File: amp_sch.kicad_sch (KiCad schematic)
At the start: 10 parts, among them IC1 AD7730, U1 74LVC125APW,118

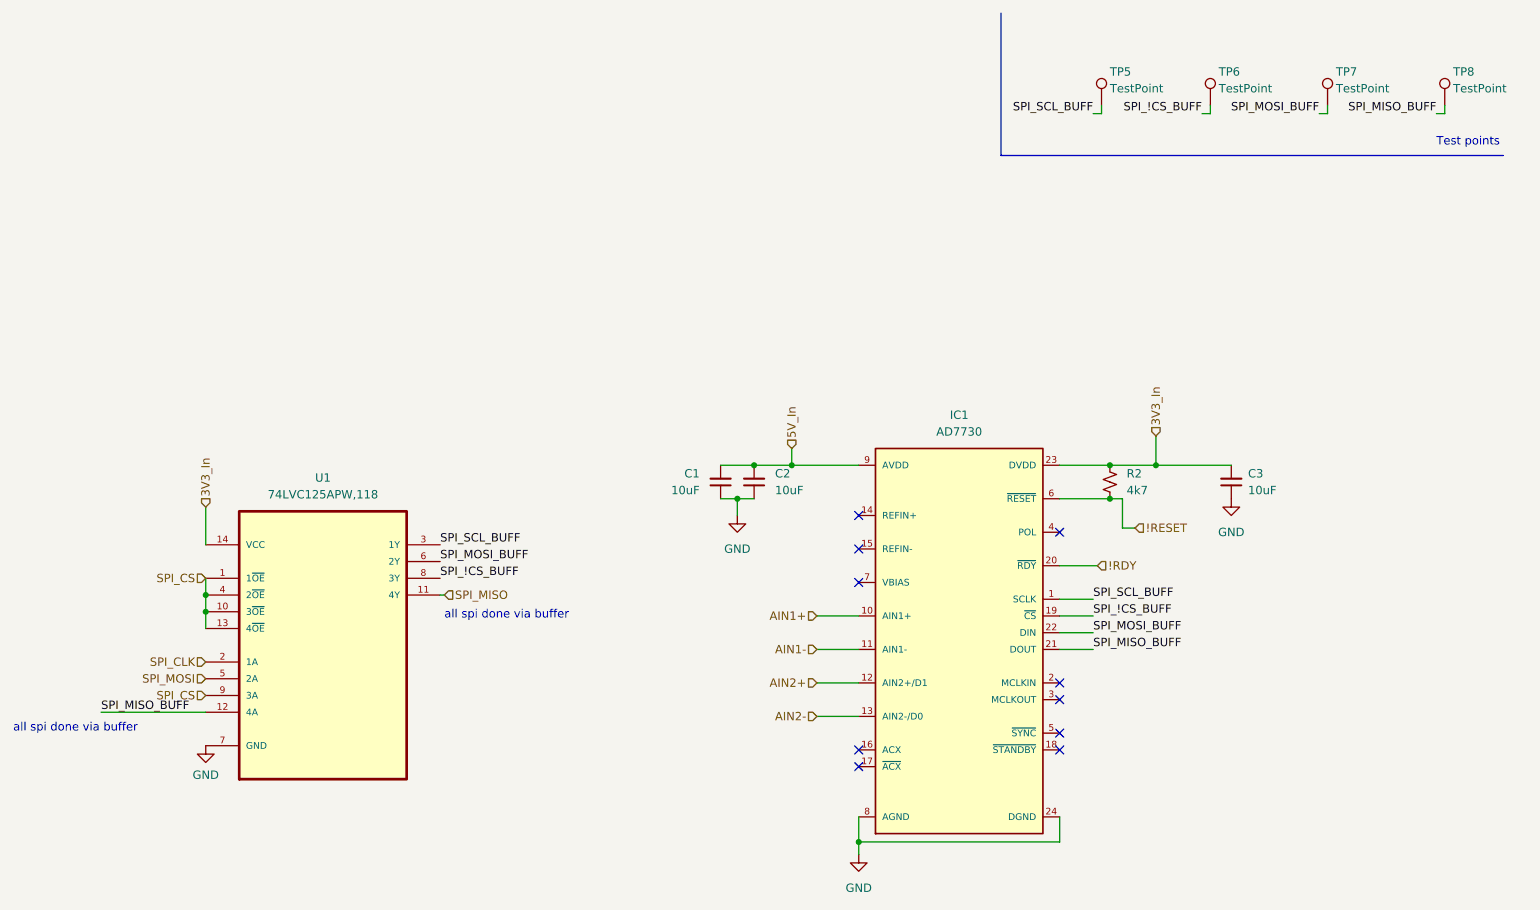
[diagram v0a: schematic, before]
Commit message: Changes to the AD7730 based on Montso's working Arduino system
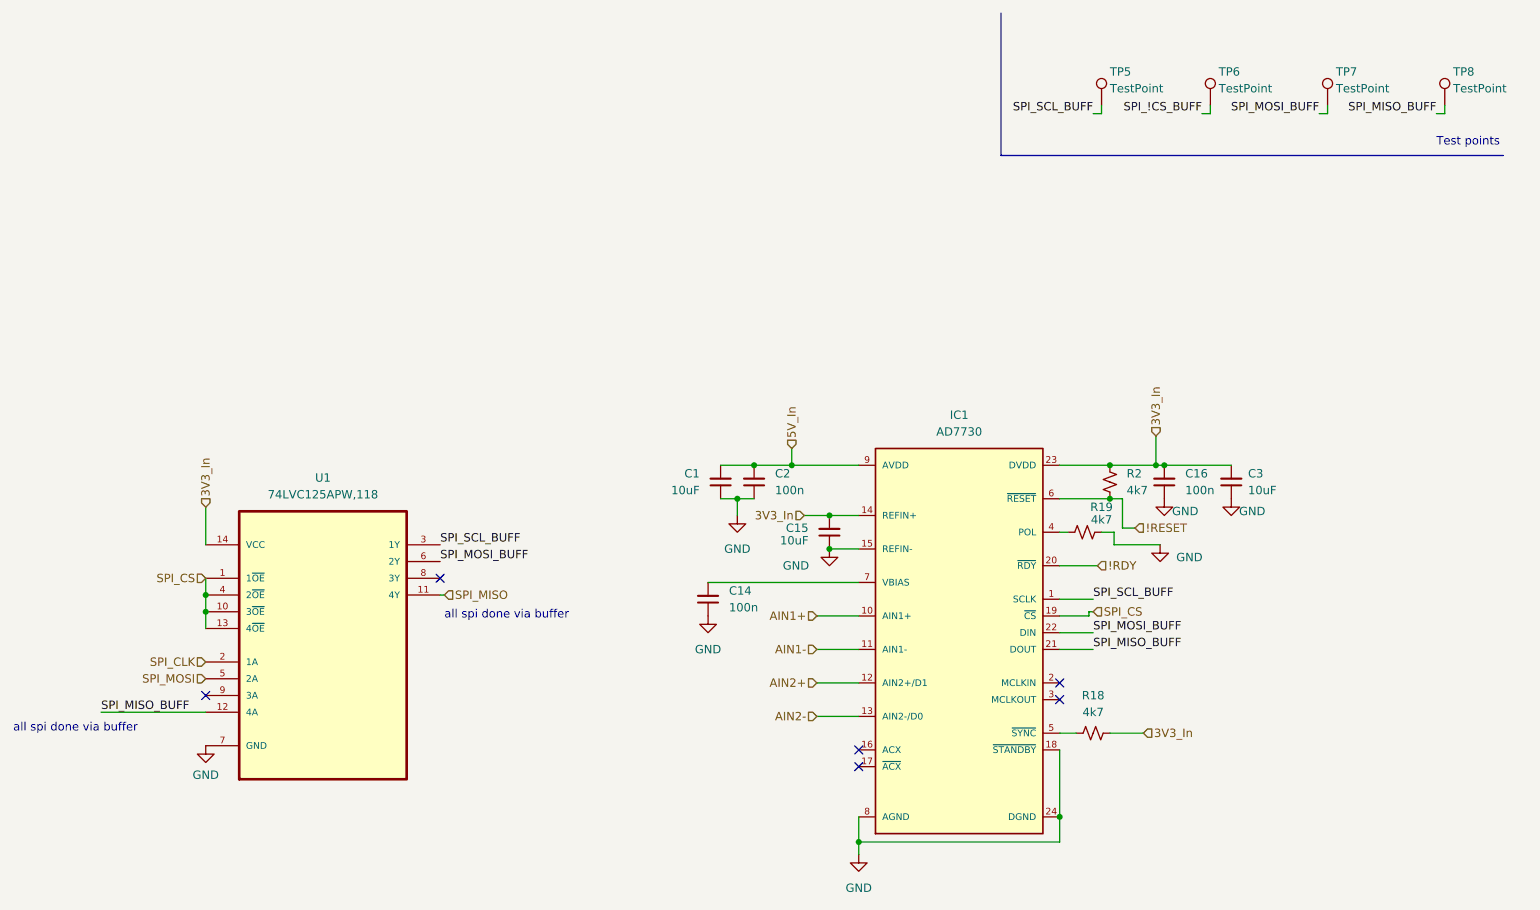
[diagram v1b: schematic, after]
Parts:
- added C14, C16: 100n, Capacitor_SMD:C_0603_1608Metric, symbol Device:C_Small
- added C15: 10uF, Capacitor_SMD:C_0603_1608Metric, symbol Device:C_Small
- added R18, R19: 4k7, Resistor_SMD:R_0402_1005Metric, symbol Device:R_Small_US
- C2: value 10uF -> 100n; LCSC C96446 -> (none); Price 0.024 -> (none)
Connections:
- net 3V3_In: now also IC1.14 (REFIN+), C15.2, C16.2, R18.1
- net GND: now also IC1.15 (REFIN-), IC1.18 (~{STANDBY}), C14.1, C15.1, C16.1, R19.1
- net SPI_!CS_BUFF: no longer IC1.19 (~{CS}), U1.8 (3Y)
- net SPI_CS: now also IC1.19 (~{CS}); no longer U1.9 (3A)
- net at IC1.4 (POL): now also R19.2
- net at IC1.5 (~{SYNC}): now also R18.2
- net at IC1.7 (VBIAS): now also C14.2
- no-connect marks 10 -> 6

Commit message: Changes made to the AD7730 circuit. HX711 circuit added and AD7730 sidestepped.
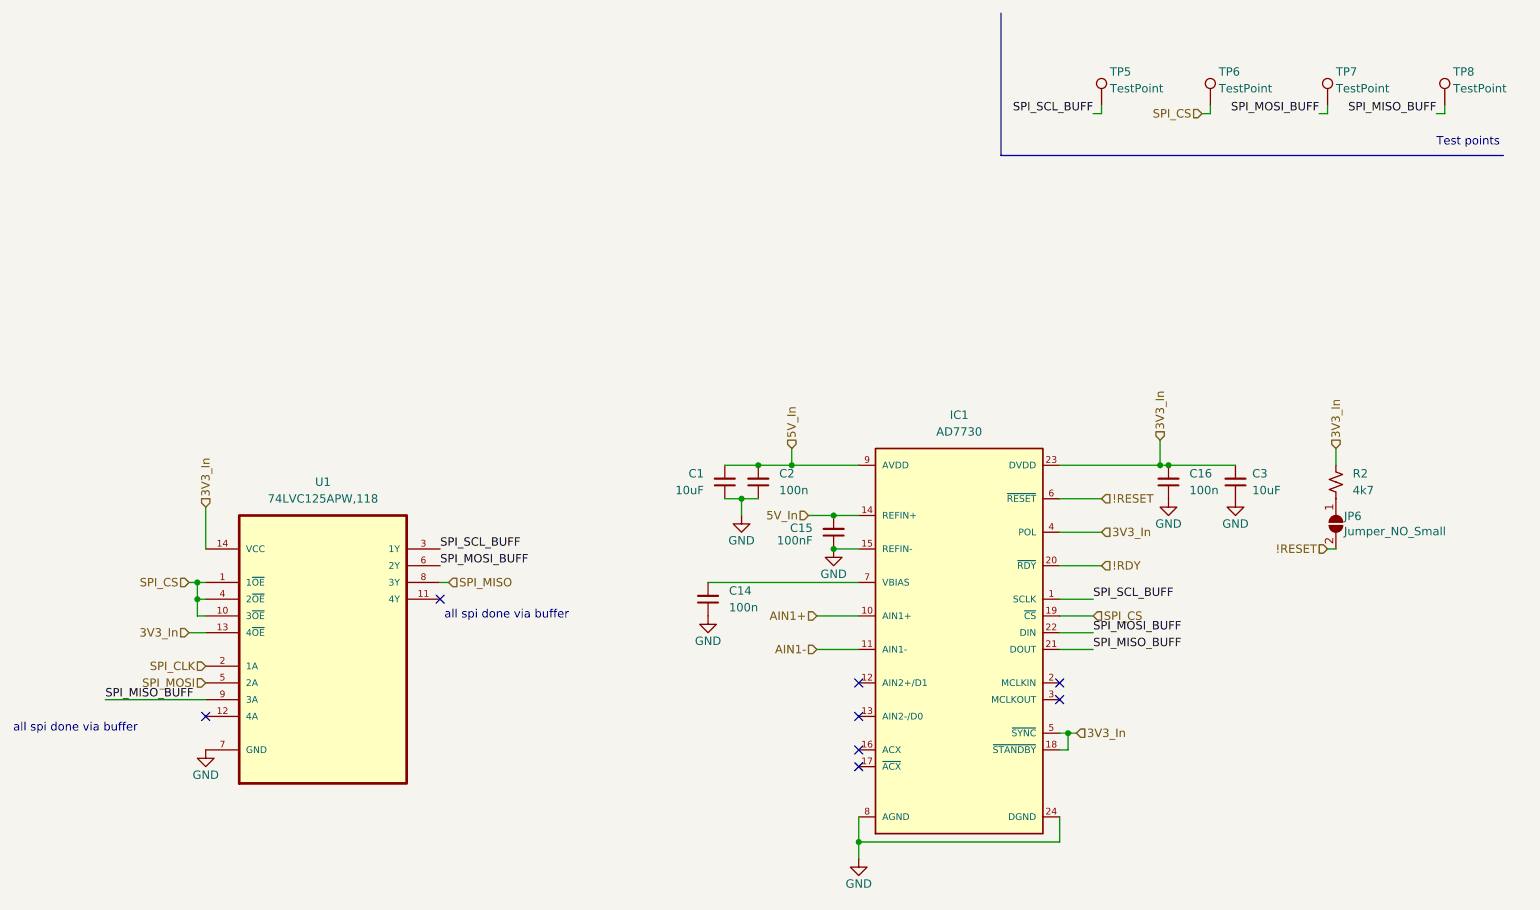
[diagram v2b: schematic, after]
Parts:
- removed R18, R19: 4k7, Resistor_SMD:R_0402_1005Metric, symbol Device:R_Small_US
- added JP6: Jumper_NO_Small, Jumper:SolderJumper-2_P1.3mm_Open_RoundedPad1.0x1.5mm, symbol Jumper:SolderJumper_2_Open
- C15: value 10uF -> 100nF
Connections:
- net SPI_!CS_BUFF is gone; now on net SPI_CS: TP6.1
- net !RESET: now also JP6.2 (B); no longer R2.1
- net 3V3_In: now also IC1.18 (~{STANDBY}), IC1.4 (POL), IC1.5 (~{SYNC}), U1.13 (4~{OE}); no longer C15.2, IC1.14 (REFIN+)
- net 5V_In: now also C15.2, IC1.14 (REFIN+)
- net GND: no longer IC1.18 (~{STANDBY})
- net SPI_CS: no longer U1.13 (4~{OE})
- net SPI_MISO: now also U1.8 (3Y); no longer U1.11 (4Y)
- net SPI_MISO_BUFF: now also U1.9 (3A); no longer U1.12 (4A)
- net AIN2+: no longer names the net of IC1.12 (AIN2+/D1)
- net AIN2-: no longer names the net of IC1.13 (AIN2-/D0)
- new net: JP6.1 (A), R2.1
- no-connect marks 6 -> 8
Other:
- moved on the sheet: C1, C15, C16, C2, C3, R2, U1

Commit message: Added footprints for HX711 circuit on PCB and modified pin assignment
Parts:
- U1: symbol 74LVC125A:74LVC125APW,118 -> 74LVC125APW_118:74LVC125APW,118
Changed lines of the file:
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@@
     )
   )
-  (symbol (lib_id "74LVC125A:74LVC125APW,118") (at 102.87 107.95 0) (unit 1)
+  (symbol (lib_id "74LVC125APW_118:74LVC125APW,118") (at 102.87 107.95 0) (unit 1)
     (in_bom yes) (on_board yes) (dnp no) (fields_autoplaced)
     (property "Reference" "U1" (at 102.87 85.09 0)

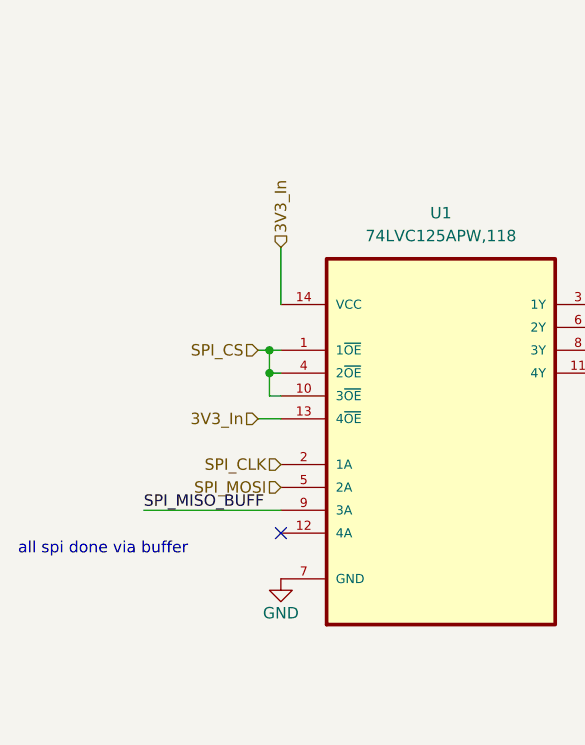
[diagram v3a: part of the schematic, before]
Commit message: Updated +3V3 tracks on pcb and buffer schematic
-Added decoupling cap for buffer
-Tied unused buffer input 4 to gnd
-Did all +3V3 connections
-Fixed +5V tracks
-gnd stitching
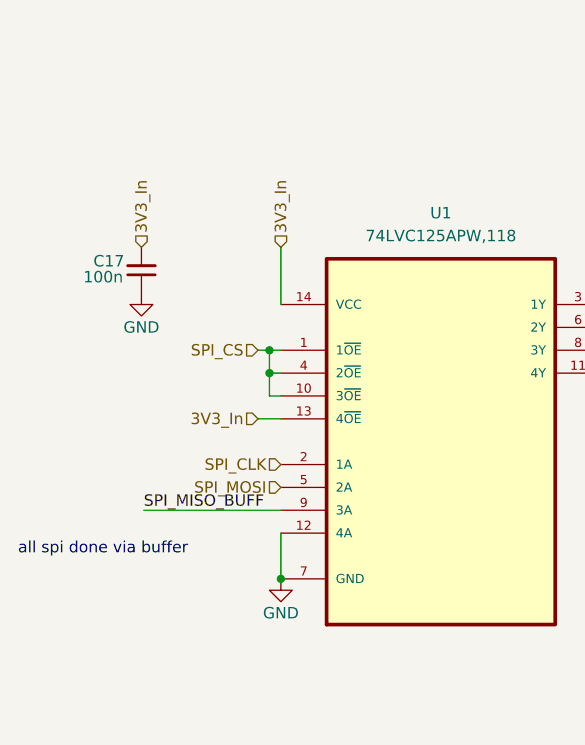
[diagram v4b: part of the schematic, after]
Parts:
- added C17: 100n, Capacitor_SMD:C_0603_1608Metric, symbol Device:C_Small
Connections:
- net 3V3_In: now also C17.2
- net GND: now also U1.12 (4A), C17.1
- no-connect marks 8 -> 7
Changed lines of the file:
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@@
   (junction (at 166.37 87.63) (diameter 0) (color 0 0 0 0)
+  )
+  (junction (at 85.09 125.73) (diameter 0) (color 0 0 0 0)
   )
   (junction (at 83.82 102.87) (diameter 0) (color 0 0 0 0)
@@
   (no_connect (at 184.15 125.73))
   (no_connect (at 120.65 102.87))
-  (no_connect (at 85.09 120.65))
   (no_connect (at 184.15 120.65))
   (no_connect (at 184.15 115.57))
@@
     (stroke (width 0) (type default))
   )
+  (wire (pts (xy 85.09 120.65) (xy 85.09 125.73))
+    (stroke (width 0) (type default))
+  )
   (wire (pts (xy 166.37 87.63) (xy 166.37 90.17))
     (stroke (width 0) (type default))
@@
   (hierarchical_label "!RESET" (shape input) (at 255.27 95.25 180) (fields_autoplaced)
     (effects (font (size 1.27 1.27)) (justify right))
+  )
+  (hierarchical_label "3V3_In" (shape input) (at 69.596 88.9 90) (fields_autoplaced)
+    (effects (font (size 1.27 1.27)) (justify left))
   )
   (hierarchical_label "3V3_In" (shape input) (at 256.54 80.01 90) (fields_autoplaced)
@@
     )
   )
+  (symbol (lib_id "power:GND") (at 69.596 93.98 0) (unit 1)
+    (in_bom yes) (on_board yes) (dnp no)
+    (property "Reference" "#PWR07" (at 69.596 100.33 0)
+      (effects (font (size 1.27 1.27)) hide)
+    )
+    (property "Value" "GND" (at 69.596 97.79 0)
+      (effects (font (size 1.27 1.27)))
+    )
+    (property "Footprint" "" (at 69.596 93.98 0)
+      (effects (font (size 1.27 1.27)) hide)
+    )
+    (property "Datasheet" "" (at 69.596 93.98 0)
+      (effects (font (size 1.27 1.27)) hide)
+    )
+    (pin "1")
+    (instances
+      (project "Pi HAT"
+        (path "/48f827a8-6e22-4a2e-abdc-c2a03098d883"
+          (reference "#PWR07") (unit 1)
+        )
+        (path "/48f827a8-6e22-4a2e-abdc-c2a03098d883/5ec412a6-29a4-46a1-a19b-d00a58557335"
+          (reference "#PWR067") (unit 1)
+        )
+      )
+    )
+  )
   (symbol (lib_id "power:GND") (at 180.34 95.25 0) (unit 1)
     (in_bom yes) (on_board yes) (dnp no)
@@
         )
       )
+    )
+  )
+  (symbol (lib_id "Device:C_Small") (at 69.596 91.44 0) (mirror x) (unit 1)
+    (in_bom yes) (on_board yes) (dnp no)
+    (property "Reference" "C17" (at 67.691 90.4304 0)
+      (effects (font (size 1.27 1.27)) (justify right))
+    )
+    (property "Value" "100n" (at 67.564 92.202 0)
+      (effects (font (size 1.27 1.27)) (justify right))
+    )
+    (property "Footprint" "Capacitor_SMD:C_0603_1608Metric" (at 69.596 91.44 0)
+      (effects (font (size 1.27 1.27)) hide)
+    )
+    (property "Datasheet" "~" (at 69.596 91.44 0)
+      (effects (font (size 1.27 1.27)) hide)
+    )
+    (property "Extended" "0" (at 69.596 91.44 0)
+      (effects (font (size 1.27 1.27)) hide)
+    )
+    (property "LCSC" "" (at 69.596 91.44 0)
+      (effects (font (size 1.27 1.27)) hide)
+    )
+    (property "Populate" "1" (at 69.596 91.44 0)
+      (effects (font (size 1.27 1.27)) hide)
+    )
+    (property "Price" "" (at 69.596 91.44 0)
+      (effects (font (size 1.27 1.27)) hide)
+    )
+    (pin "1")
+    (pin "2")
+    (instances
+      (project "Pi HAT"
+        (path "/48f827a8-6e22-4a2e-abdc-c2a03098d883/5ec412a6-29a4-46a1-a19b-d00a58557335"
+          (reference "C17") (unit 1)
+        )
+      )

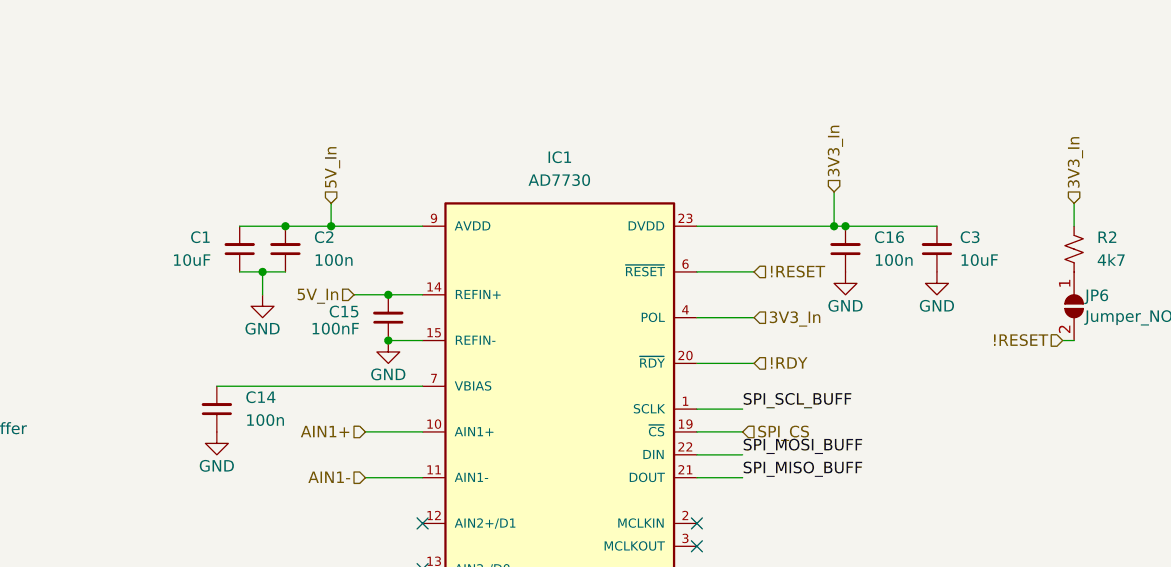
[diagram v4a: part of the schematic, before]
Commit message: Fixed HX711 decoupling cap. Changed EXC+.
- Changed EXC+ to 4.06V
- Consistent values for schematic components
- Added B.silkscreen art
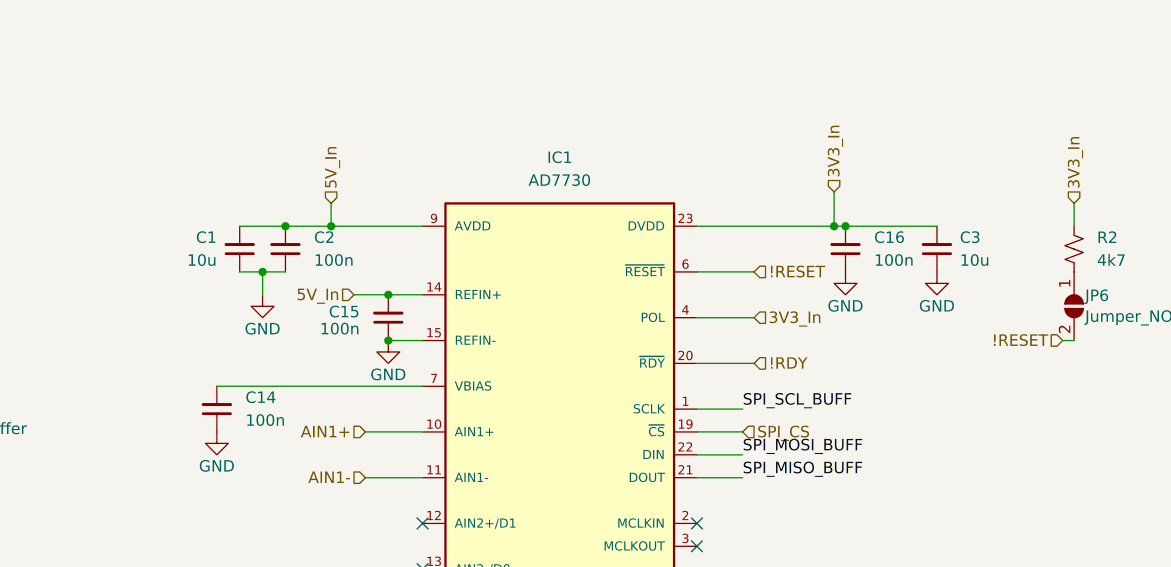
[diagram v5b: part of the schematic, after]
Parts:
- C1, C3: value 10uF -> 10u
- C15: value 100nF -> 100n
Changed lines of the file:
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@@
   (symbol (lib_id "Device:C_Small") (at 241.3 85.09 180) (unit 1)
     (in_bom yes) (on_board yes) (dnp no) (fields_autoplaced)
-    (property "Reference" "C3" (at 243.84 83.8135 0)
-      (effects (font (size 1.27 1.27)) (justify right))
-    )
-    (property "Value" "10uF" (at 243.84 86.3535 0)
+    (property "Reference" "C3" (at 243.84 83.8136 0)
+      (effects (font (size 1.27 1.27)) (justify right))
+    )
+    (property "Value" "10u" (at 243.84 86.3536 0)
       (effects (font (size 1.27 1.27)) (justify right))
     )
@@
       (effects (font (size 1.27 1.27)) (justify right))
     )
-    (property "Value" "100nF" (at 177.165 93.9735 0)
+    (property "Value" "100n" (at 177.165 93.9735 0)
       (effects (font (size 1.27 1.27)) (justify right))
     )
@@
   (symbol (lib_id "Device:C_Small") (at 163.83 85.09 0) (mirror x) (unit 1)
     (in_bom yes) (on_board yes) (dnp no) (fields_autoplaced)
-    (property "Reference" "C1" (at 160.655 83.8135 0)
-      (effects (font (size 1.27 1.27)) (justify right))
-    )
-    (property "Value" "10uF" (at 160.655 86.3535 0)
-      (effects (font (size 1.27 1.27)) (justify right))
-    )
+    (property "Reference" "C1" (at 161.29 83.8136 0)
+      (effects (font (size 1.27 1.27)) (justify right))
+    )
+    (property "Value" "10u" (at 161.29 86.3536 0)
+      (effects (font (size 1.27 1.27)) (justify right))
+    )
